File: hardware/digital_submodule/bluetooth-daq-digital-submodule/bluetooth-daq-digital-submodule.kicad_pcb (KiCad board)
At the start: 2 copper layers, 150 x 150.9 mm, 142 parts, among them J1 MCU I/F, J2 Digital Inputs, J3 Digital Outputs, J4 Communication I/F, J5 RS-485 I/F, U1 74HC595, U2 74HC595, U3 74HC165, U4 74HC165, U5 24LC1025, U6 SN75176AD, U7 CD4053B, U8 CD4053B

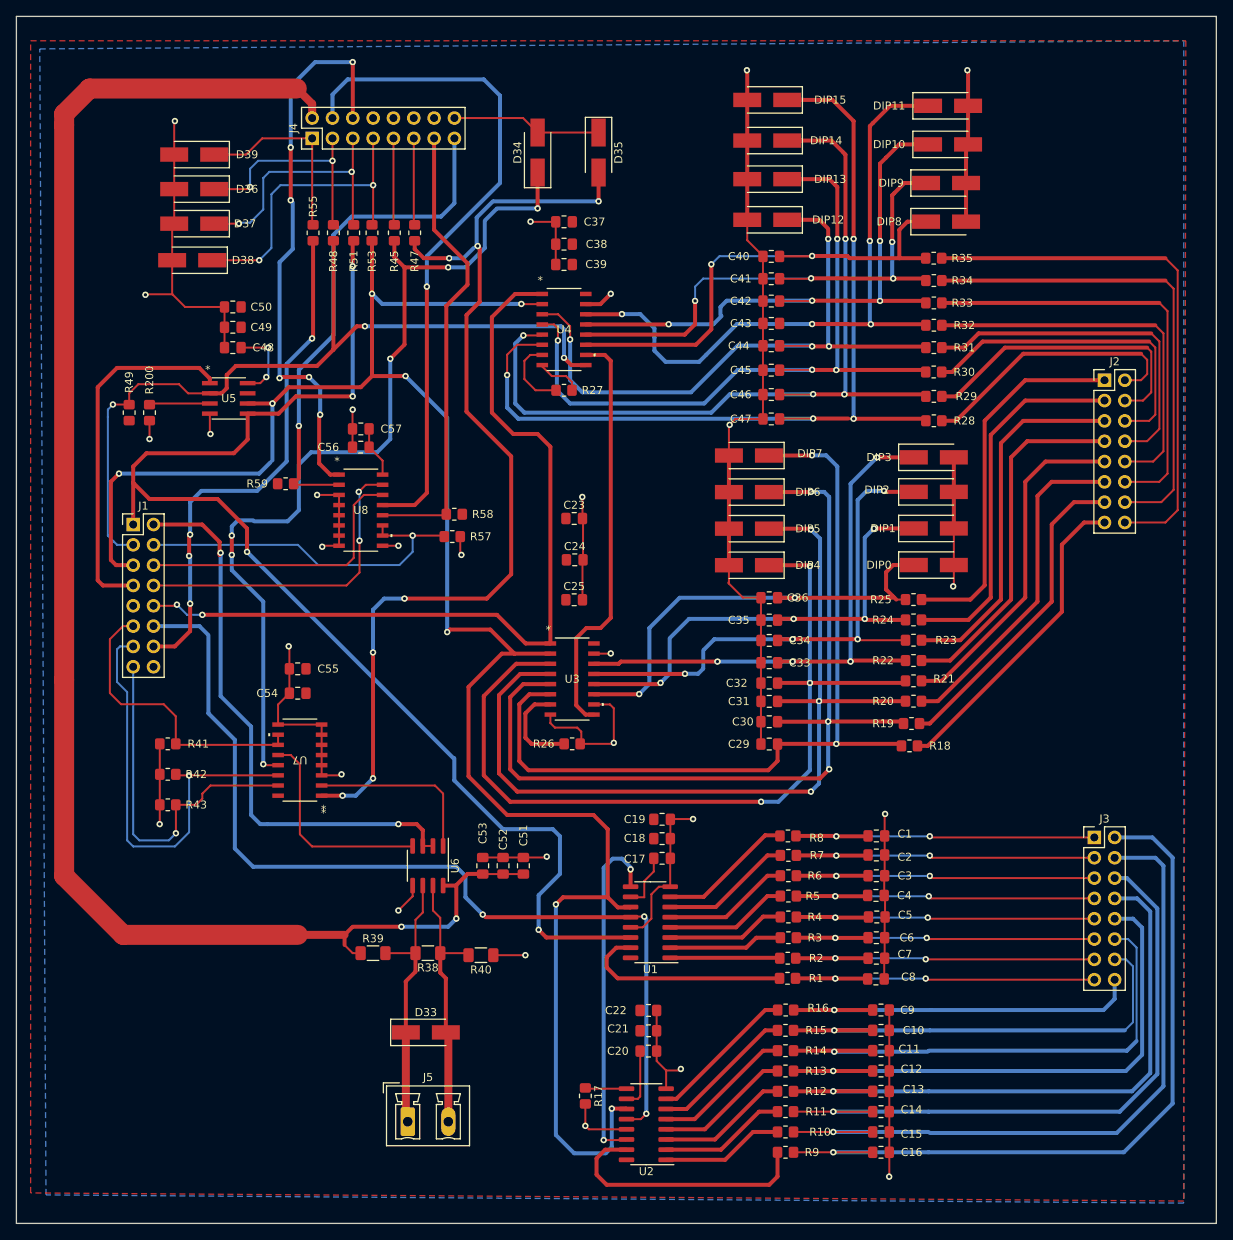
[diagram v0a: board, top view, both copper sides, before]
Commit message: Resolved PCB design errors
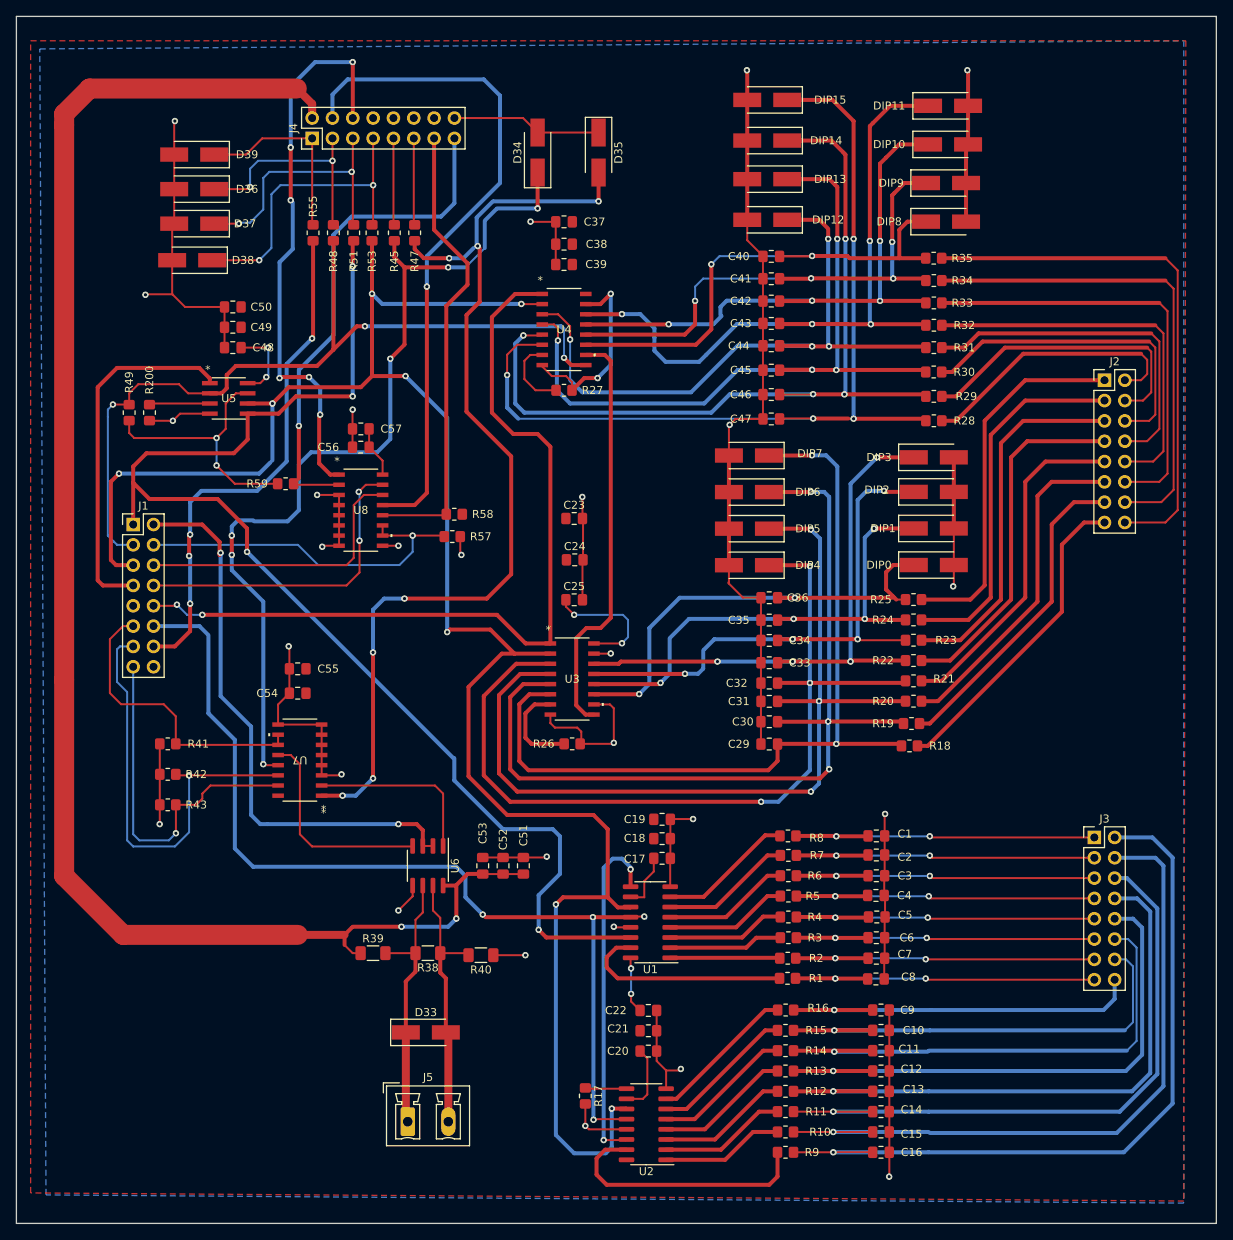
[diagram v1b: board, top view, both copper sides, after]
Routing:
- net 3V3: track 30.9 -> 87.9 mm, vias 2 -> 8
- net GND: track 392.2 -> 403.6 mm, vias 29 -> 30
- net Net-(C43-Pad2): track 81.8 -> 85.9 mm
- net DO_LOAD: track 119.2 -> 121.6 mm, vias 3 -> 4
